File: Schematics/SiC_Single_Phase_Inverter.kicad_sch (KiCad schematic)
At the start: 4 parts, among them J1 23AH8785-Black, J2 23AH8786-Red, J3 23AH8786-Red, J4 23AH8785-Black

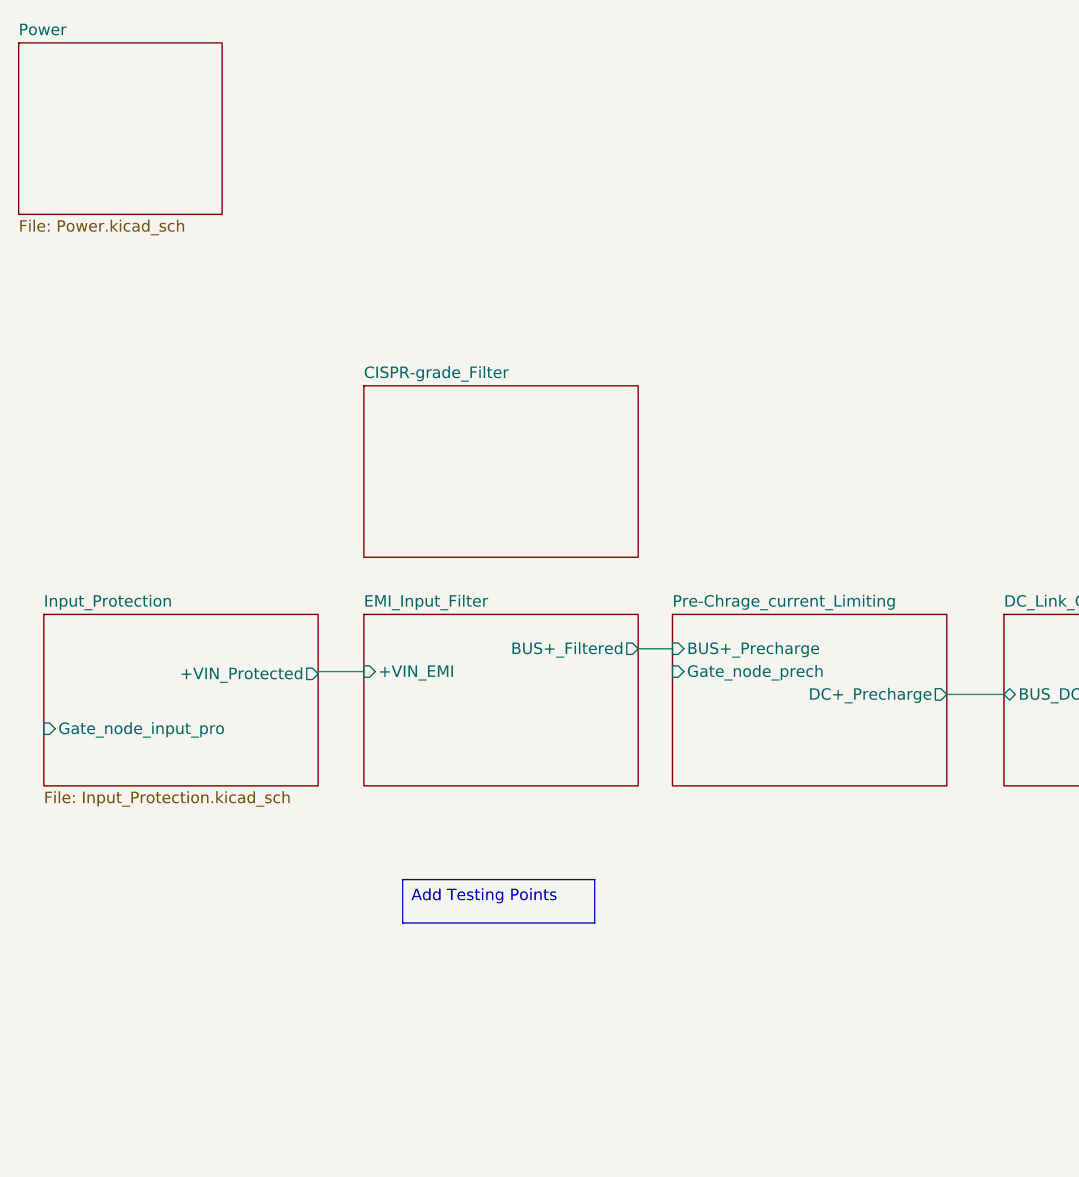
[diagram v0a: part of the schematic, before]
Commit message: [WIP SiC Single Phase Inverter]
- Added AC - DC converter for 15V isolated supply
- Added 2x IRM-05 to the power sub sheet
- Added 3D part for the IRM-05
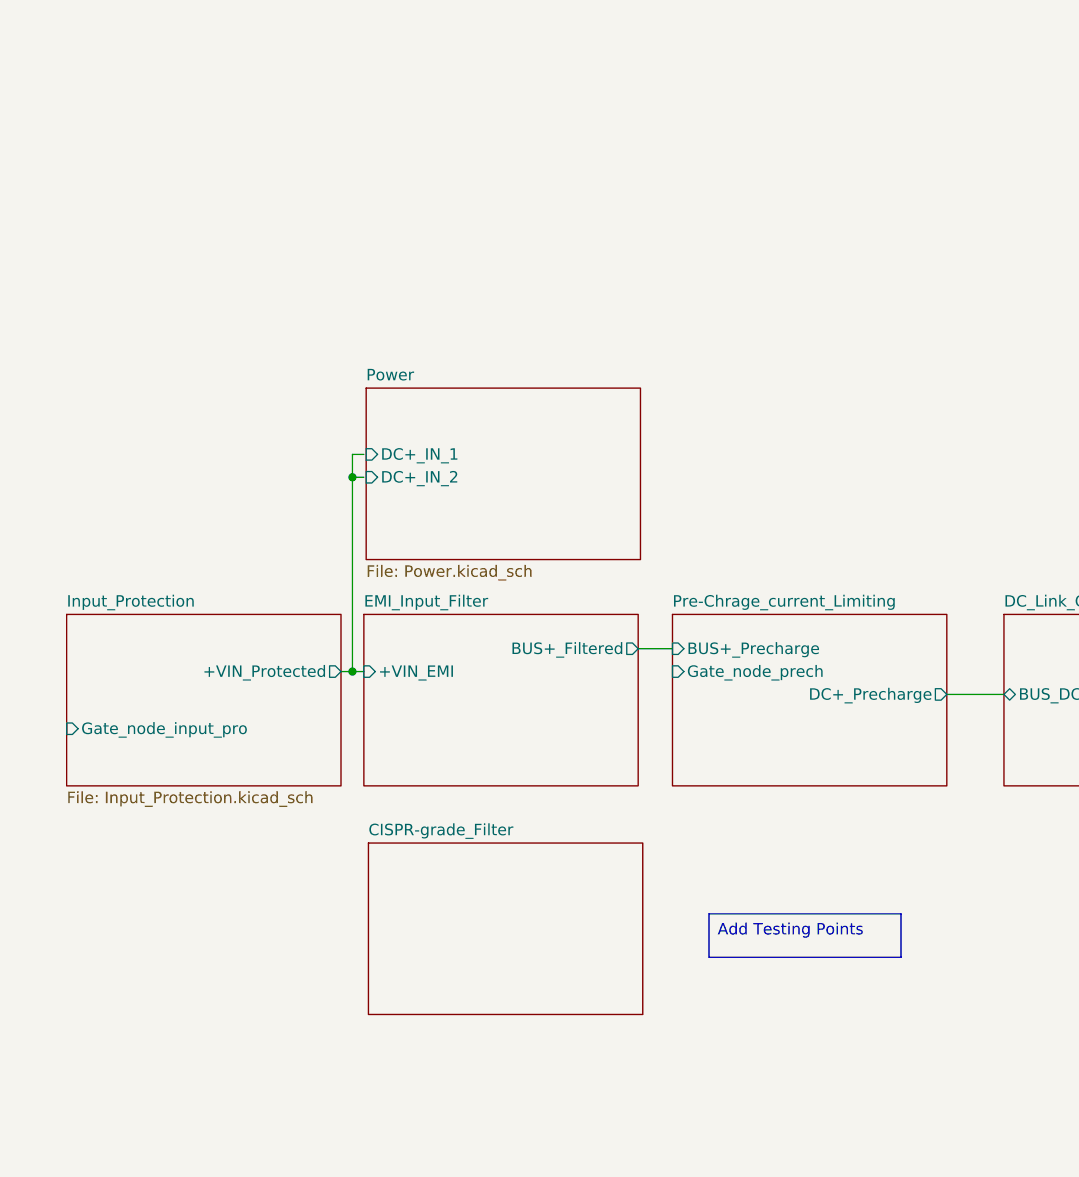
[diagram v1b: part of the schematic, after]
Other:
- sheet Power ports: added DC+_IN_1, DC+_IN_2; removed none
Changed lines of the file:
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@@
 	(text_box "Add Testing Points"
 		(exclude_from_sim no)
-		(at 65.278 114.554 0)
+		(at 99.314 118.364 0)
 		(size 21.336 4.826)
 		(margins 0.9525 0.9525 0.9525 0.9525)
@@
 		)
 	)
+	(junction
+		(at 59.69 91.44)
+		(diameter 0)
+		(color 0 0 0 0)
+	)
+	(junction
+		(at 59.69 69.85)
+		(diameter 0)
+		(color 0 0 0 0)
+	)
 	(wire
 		(pts
@@
 	(wire
 		(pts
+			(xy 60.96 67.31) (xy 59.69 67.31)
+		)
+		(stroke
+			(width 0)
+			(type default)
+		)
+	)
+	(wire
+		(pts
 			(xy 228.6 74.93) (xy 231.14 74.93)
 		)
@@
 		)
 	)
+	(wire
+		(pts
+			(xy 59.69 91.44) (xy 60.96 91.44)
+		)
+		(stroke
+			(width 0)
+			(type default)
+		)
+	)
 	(polyline
 		(pts
@@
 	(wire
 		(pts
+			(xy 58.42 91.44) (xy 59.69 91.44)
+		)
+		(stroke
+			(width 0)
+			(type default)
+		)
+	)
+	(wire
+		(pts
 			(xy 91.44 88.9) (xy 95.25 88.9)
 		)
@@
 	(wire
 		(pts
-			(xy 55.88 91.44) (xy 60.96 91.44)
+			(xy 261.62 76.2) (xy 265.43 76.2)
 		)
 		(stroke
@@
 	(wire
 		(pts
-			(xy 261.62 76.2) (xy 265.43 76.2)
+			(xy 228.6 78.74) (xy 231.14 78.74)
 		)
 		(stroke
@@
 	(wire
 		(pts
-			(xy 228.6 78.74) (xy 231.14 78.74)
+			(xy 60.96 69.85) (xy 59.69 69.85)
 		)
 		(stroke
@@
 		(pts
 			(xy 201.93 95.25) (xy 204.47 95.25)
+		)
+		(stroke
+			(width 0)
+			(type default)
+		)
+	)
+	(wire
+		(pts
+			(xy 59.69 69.85) (xy 59.69 91.44)
+		)
+		(stroke
+			(width 0)
+			(type default)
+		)
+	)
+	(wire
+		(pts
+			(xy 59.69 67.31) (xy 59.69 69.85)
 		)
 		(stroke
@@
 	)
 	(sheet
-		(at 60.96 59.69)
+		(at 61.468 110.49)
 		(size 30.48 19.05)
 		(exclude_from_sim no)
@@
 		)
 		(property "Sheetname" "CISPR‑grade_Filter"
-			(at 60.96 58.9784 0)
+			(at 61.468 109.7784 0)
 			(effects
 				(font
@@
 		)
 		(property "Sheetfile" "CISPR‑grade_Filter.kicad_sch"
-			(at 60.96 79.3246 0)
+			(at 61.468 130.1246 0)
 			(effects
 				(font
@@
 	)
 	(sheet
-		(at 25.4 85.09)
+		(at 27.94 85.09)
 		(size 30.48 19.05)
 		(exclude_from_sim no)
@@
 		)
 		(property "Sheetname" "Input_Protection"
-			(at 25.4 84.3784 0)
+			(at 27.94 84.3784 0)
 			(effects
 				(font
@@
 		)
 		(property "Sheetfile" "Input_Protection.kicad_sch"
-			(at 25.4 104.7246 0)
+			(at 27.94 104.7246 0)
 			(effects
 				(font
@@
 		)
 		(pin "+VIN_Protected" output
-			(at 55.88 91.694 0)
+			(at 58.42 91.44 0)
 			(effects
 				(font
@@
 		)
 		(pin "Gate_node_input_pro" input
-			(at 25.4 97.79 180)
+			(at 27.94 97.79 180)
 			(effects
 				(font
@@
 	)
 	(sheet
-		(at 22.606 21.59)
-		(size 22.606 19.05)
+		(at 61.214 59.944)
+		(size 30.48 19.05)
 		(exclude_from_sim no)
 		(in_bom yes)
@@
 		)
 		(property "Sheetname" "Power"
-			(at 22.606 20.8784 0)
+			(at 61.214 59.2324 0)
 			(effects
 				(font
@@
 		)
 		(property "Sheetfile" "Power.kicad_sch"
-			(at 22.606 41.2246 0)
+			(at 61.214 79.5786 0)
 			(effects
 				(font
@@
 			)
 		)
+		(pin "DC+_IN_1" input
+			(at 61.214 67.31 180)
+			(effects
+				(font
+					(size 1.27 1.27)
+				)
+				(justify left)
+			)
+		)
+		(pin "DC+_IN_2" input
+			(at 61.214 69.85 180)
+			(effects
+				(font
+					(size 1.27 1.27)
+				)
+				(justify left)
+			)
+		)

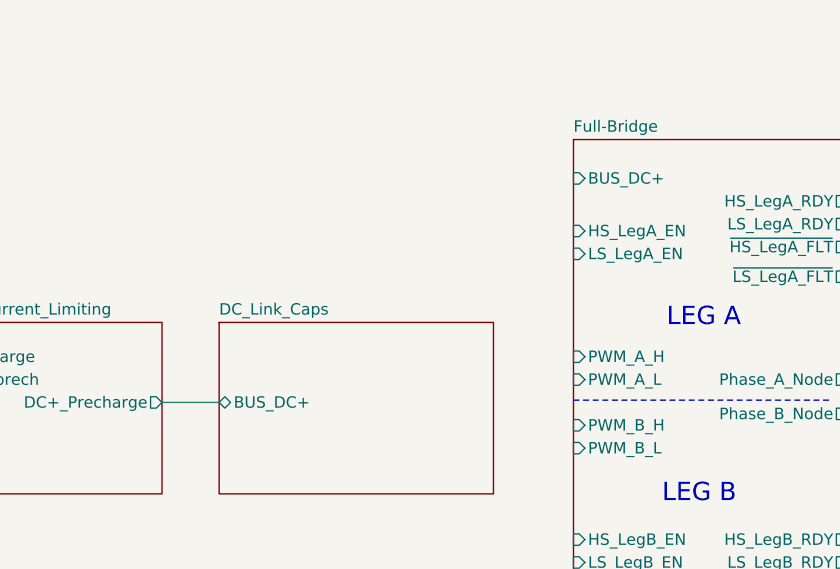
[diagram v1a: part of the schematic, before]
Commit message: [WIP Single Phase SiC Inverter]
- Added molex 4 pin pcb connector for +15V power
- Added 3d model, symbol and footprint
- Added datasheet for molex connector
- Added Male and Female pcb - pcb connectors to all sub sheets
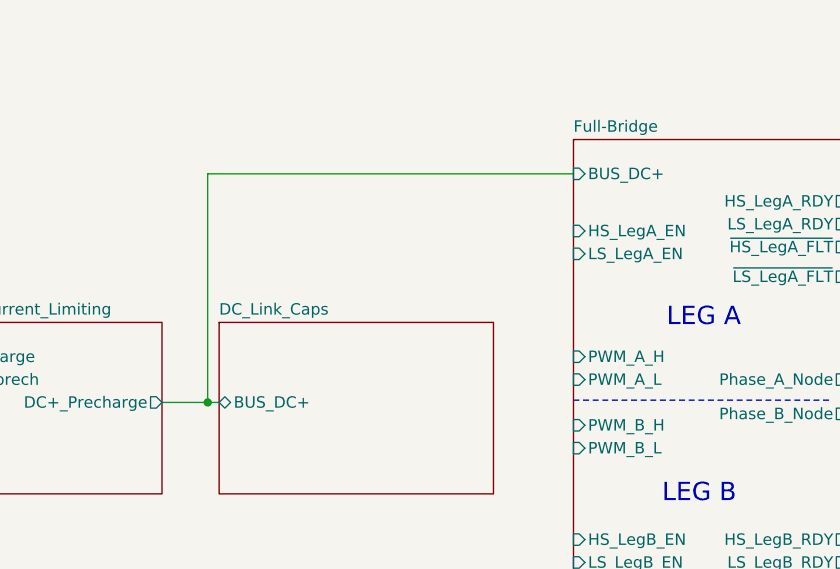
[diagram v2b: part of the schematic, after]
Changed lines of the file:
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@@
+	)
+	(junction
+		(at 130.81 93.98)
+		(diameter 0)
+		(color 0 0 0 0)
 	)
 	(junction
@@
 	(wire
 		(pts
+			(xy 130.81 93.98) (xy 132.08 93.98)
+		)
+		(stroke
+			(width 0)
+			(type default)
+		)
+	)
+	(wire
+		(pts
 			(xy 261.62 80.01) (xy 265.43 80.01)
 		)
@@
 	(wire
 		(pts
+			(xy 130.81 68.58) (xy 130.81 93.98)
+		)
+		(stroke
+			(width 0)
+			(type default)
+		)
+	)
+	(wire
+		(pts
 			(xy 59.69 91.44) (xy 60.96 91.44)
 		)
@@
 	(wire
 		(pts
+			(xy 171.45 68.58) (xy 130.81 68.58)
+		)
+		(stroke
+			(width 0)
+			(type default)
+		)
+	)
+	(wire
+		(pts
 			(xy 91.44 88.9) (xy 95.25 88.9)
 		)
@@
 	(wire
 		(pts
-			(xy 125.73 93.98) (xy 132.08 93.98)
+			(xy 125.73 93.98) (xy 130.81 93.98)
 		)
 		(stroke
@@
 		)
 		(pin "BUS_DC+" input
-			(at 171.45 69.088 180)
-			(effects
-				(font
+			(at 171.45 68.58 180)
+			(effects
+				(font

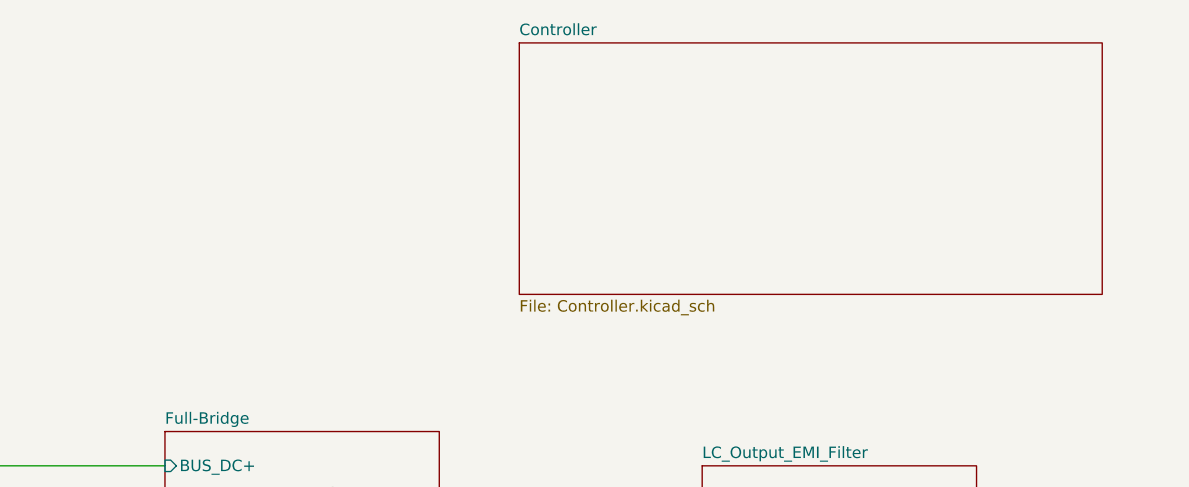
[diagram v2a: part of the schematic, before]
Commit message: [WIP SiC Single Phase Inverter]
- Updated README to have a Block Diagram
- WIP Sub sheets Power, Controller
- Added the F2800 controller to the project
- Added the controller to the controller sub sheet
- Added text for a 15V to 3V3 voltage converter
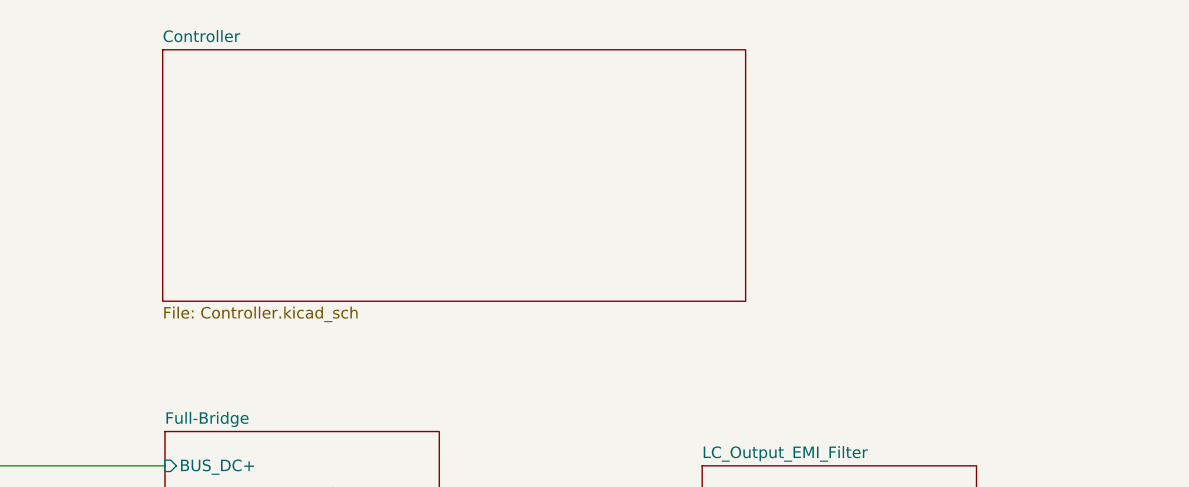
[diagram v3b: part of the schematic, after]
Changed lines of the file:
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@@
 	)
 	(sheet
-		(at 210.82 21.59)
+		(at 171.196 22.352)
 		(size 64.77 27.94)
 		(exclude_from_sim no)
@@
 		)
 		(property "Sheetname" "Controller"
-			(at 210.82 20.8784 0)
+			(at 171.196 21.6404 0)
 			(effects
 				(font
@@
 		)
 		(property "Sheetfile" "Controller.kicad_sch"
-			(at 210.82 50.1146 0)
+			(at 171.196 50.8766 0)
 			(effects
 				(font

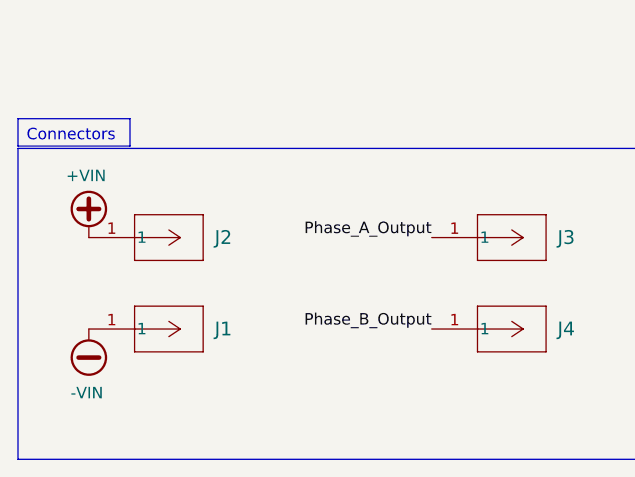
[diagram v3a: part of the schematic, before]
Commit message: [WIP Single Phase Inverter]
- Changed all Refs within each sub sheet (Stripe)
- Added 3V3 Power Supply off of 15V iso supply
- Added footprint, symbol and 3d part
- updated PCB with new part
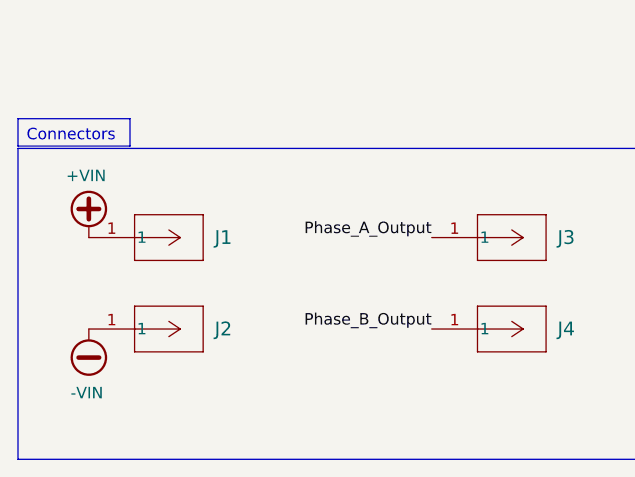
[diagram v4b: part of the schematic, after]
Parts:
- renumbered J2 to J1, J1 to J2
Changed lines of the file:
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@@
 		(dnp no)
 		(fields_autoplaced yes)
-		(property "Reference" "J1"
+		(property "Reference" "J2"
 			(at 48.26 172.7199 0)
 			(effects
@@
 			(project "SiC_Single_Phase_Inverter"
 				(path "/a1ed0539-9735-4ad1-a8fd-87e26e7fce16"
-					(reference "J1")
+					(reference "J2")
 					(unit 1)
 				)
@@
 		(on_board yes)
 		(dnp no)
-		(property "Reference" "#PWR05"
+		(property "Reference" "#PWR01"
 			(at 34.29 165.1 0)
 			(effects
@@
 			(project "SiC_Single_Phase_Inverter"
 				(path "/a1ed0539-9735-4ad1-a8fd-87e26e7fce16"
-					(reference "#PWR05")
+					(reference "#PWR01")
 					(unit 1)
 				)
@@
 		(dnp no)
 		(fields_autoplaced yes)
-		(property "Reference" "J2"
+		(property "Reference" "J1"
 			(at 48.26 162.5599 0)
 			(effects
@@
 			(project "SiC_Single_Phase_Inverter"
 				(path "/a1ed0539-9735-4ad1-a8fd-87e26e7fce16"
-					(reference "J2")
+					(reference "J1")
 					(unit 1)
 				)
@@
 		(on_board yes)
 		(dnp no)
-		(property "Reference" "#PWR01"
+		(property "Reference" "#PWR02"
 			(at 34.29 170.18 0)
 			(effects
@@
 			(project "SiC_Single_Phase_Inverter"
 				(path "/a1ed0539-9735-4ad1-a8fd-87e26e7fce16"
-					(reference "#PWR01")
-					(unit 1)
-				)
+					(reference "#PWR02")
+					(unit 1)
+				)
